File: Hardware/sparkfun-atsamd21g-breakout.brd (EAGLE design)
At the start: 17.8 x 33 mm, 41 parts, among them Q1 2N7002PW, Q3 2.5A/30V, U1 ATSAMD21G-A, U2 MIC5219 3.3V, U4 74AHC1G125

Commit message: Minor, pre-checklist modifications.
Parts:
- C5, C6: value 22pF -> 15pF; device SparkFun-Capacitors:0402-CAP -> samd21-temp:0402-CAP
- D1: value Yellow -> GREEN
- D4: value GREEN -> Yellow
- Y1: value (none) -> 32.768kHz
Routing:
- net SDA: track 9.45 -> 8.50 mm
- net D5: track 15.0 -> 14.3 mm
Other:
- board text added: "This is a 4-layer board!"

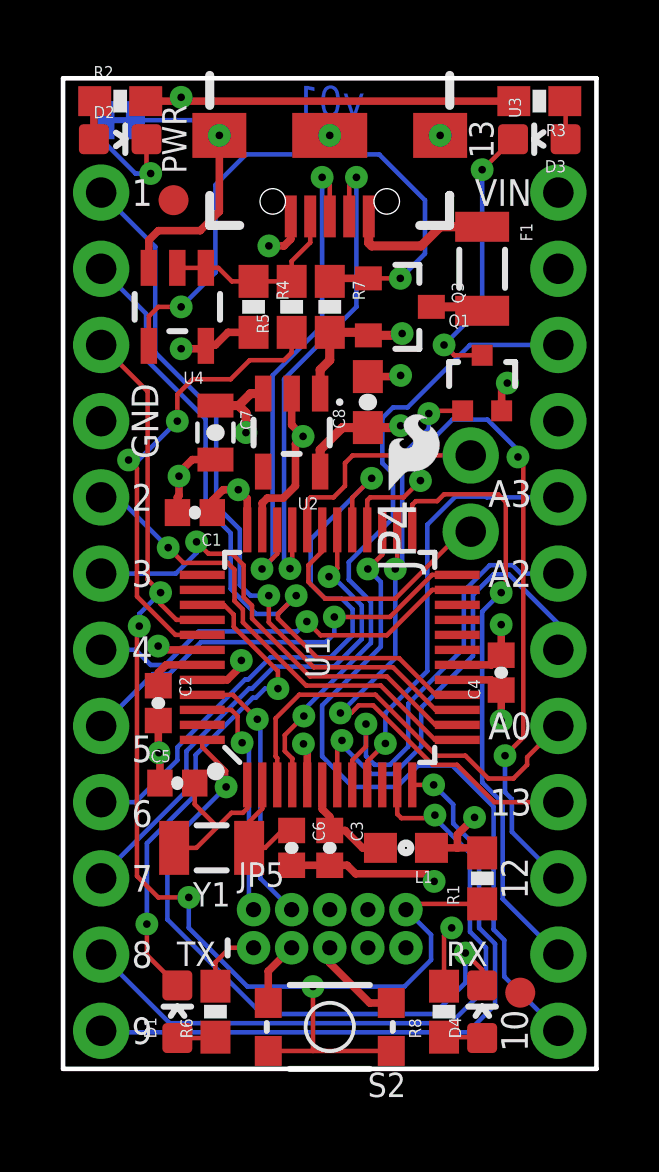
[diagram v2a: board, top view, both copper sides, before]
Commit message: Renaming U4 to U3, adding tSilk to pin 11, dimension to .008in.
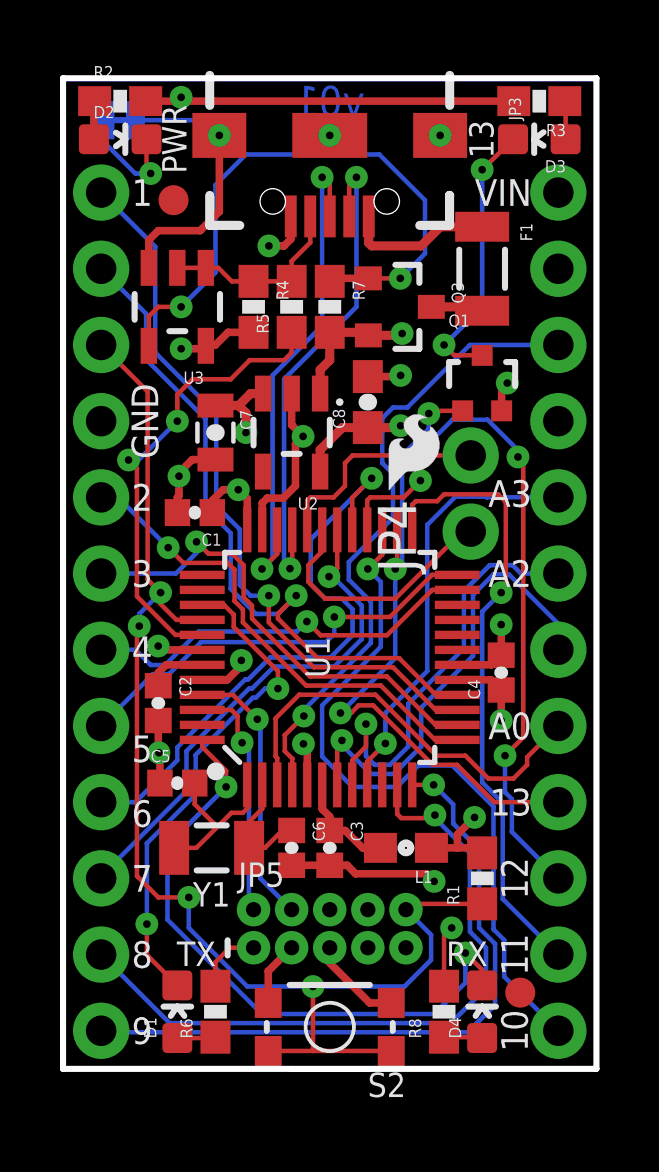
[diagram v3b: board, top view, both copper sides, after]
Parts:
- removed U4: 74AHC1G125, SparkFun-DigitalIC:SOT23-5
- added JP3: (no value), SparkFun-Connectors:USB-AB-MICRO-SMD_V03
- U3: value (none) -> 74AHC1G125; device SparkFun-Connectors:USB-AB-MICRO-SMD_V03 -> SparkFun-DigitalIC:SOT23-5
- moved U3 7.65 mm to (3.81, 25.4), turned to 180 degrees
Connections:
- net 3.3V: now also U3.5; no longer U4.5
- net GND: now also JP3.GND1, JP3.SHIELD1, JP3.SHIELD2, JP3.SHIELD3, U3.3; no longer U3.GND1, U3.SHIELD1, U3.SHIELD2, U3.SHIELD3, U4.3
- net N$1: now also JP3.VBUS1; no longer U3.VBUS1
- net N$8: now also JP3.ID1, U3.1, U3.2; no longer U3.ID1, U4.1, U4.2
- net N$9: now also U3.4; no longer U4.4
- net USB_D+: now also JP3.D+1; no longer U3.D+1
- net USB_D-: now also JP3.D-1; no longer U3.D-1
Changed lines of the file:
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@@
 <setting verticaltext="up"/>
 </settings>
-<grid distance="0.05" unitdist="inch" unit="inch" style="lines" multiple="1" display="yes" altdistance="0.0025" altunitdist="inch" altunit="inch"/>
+<grid distance="0.05" unitdist="inch" unit="inch" style="lines" multiple="1" display="yes" altdistance="0.005" altunitdist="inch" altunit="inch"/>
 <layers>
 <layer number="1" name="Top" color="4" fill="1" visible="yes" active="yes"/>
@@
 <layer number="47" name="Measures" color="7" fill="1" visible="no" active="yes"/>
 <layer number="48" name="Document" color="7" fill="1" visible="no" active="yes"/>
-<layer number="49" name="Reference" color="7" fill="1" visible="yes" active="yes"/>
+<layer number="49" name="Reference" color="7" fill="1" visible="no" active="yes"/>
 <layer number="50" name="dxf" color="7" fill="1" visible="no" active="no"/>
 <layer number="51" name="tDocu" color="6" fill="1" visible="yes" active="yes"/>
@@
 <board>
 <plain>
-<wire x1="0" y1="0" x2="0" y2="33.02" width="0.1524" layer="20"/>
-<wire x1="0" y1="33.02" x2="17.78" y2="33.02" width="0.1524" layer="20"/>
-<wire x1="17.78" y1="33.02" x2="17.78" y2="0" width="0.1524" layer="20"/>
-<wire x1="17.78" y1="0" x2="0" y2="0" width="0.1524" layer="20"/>
+<wire x1="0" y1="0" x2="0" y2="33.02" width="0.2032" layer="20"/>
+<wire x1="0" y1="33.02" x2="17.78" y2="33.02" width="0.2032" layer="20"/>
+<wire x1="17.78" y1="33.02" x2="17.78" y2="0" width="0.2032" layer="20"/>
+<wire x1="17.78" y1="0" x2="0" y2="0" width="0.2032" layer="20"/>
 <text x="2.286" y="29.21" size="0.889" layer="21" font="vector" ratio="15" align="center-left">1</text>
 <text x="2.286" y="21.59" size="0.889" layer="21" font="vector" ratio="15" rot="R270" align="bottom-center">GND</text>
@@
 <text x="8.89" y="32.766" size="1.016" layer="16" font="vector" ratio="15" rot="MR0" align="top-center">v01</text>
 <text x="8.89" y="35.56" size="0.889" layer="51" font="vector" ratio="15" align="bottom-center">This is a 4-layer board!</text>
+<text x="15.494" y="3.81" size="0.889" layer="21" font="vector" ratio="15" rot="R90" align="bottom-center">11</text>
 </plain>
 <attributes>
@@
 <attribute name="PROD_ID" value="RES-11150" x="13.97" y="26.67" size="0.889" layer="27" font="vector" ratio="15" rot="R270" display="off"/>
 </element>
-<element name="U3" library="SparkFun-Connectors" package="USB-AB-MICRO-SMD_V03" value="" x="8.89" y="31.115" rot="R270">
+<element name="JP3" library="SparkFun-Connectors" package="USB-AB-MICRO-SMD_V03" value="" x="8.89" y="31.115" rot="R270">
 <attribute name="PROD_ID" value="CONN-11794" x="8.89" y="31.115" size="0.889" layer="27" font="vector" ratio="15" rot="R270" display="off"/>
 </element>
-<element name="U4" library="SparkFun-DigitalIC" package="SOT23-5" value="74AHC1G125" x="3.81" y="25.4" rot="R180">
+<element name="U3" library="SparkFun-DigitalIC" package="SOT23-5" value="74AHC1G125" x="3.81" y="25.4" rot="R180">
 <attribute name="PROD_ID" value="IC-11920" x="3.81" y="25.4" size="0.889" layer="27" font="vector" ratio="15" rot="R180" display="off"/>
 </element>
@@
 <contactref element="JP5" pad="5"/>
 <contactref element="JP5" pad="3"/>
-<contactref element="U3" pad="GND1"/>
-<contactref element="U3" pad="SHIELD1"/>
-<contactref element="U3" pad="SHIELD2"/>
-<contactref element="U3" pad="SHIELD3"/>
-<contactref element="U4" pad="3"/>
+<contactref element="JP3" pad="GND1"/>
+<contactref element="JP3" pad="SHIELD1"/>
+<contactref element="JP3" pad="SHIELD2"/>
+<contactref element="JP3" pad="SHIELD3"/>
+<contactref element="U3" pad="3"/>
 <via x="8.001" y="21.082" extent="1-16" drill="0.254"/>
 <via x="11.2522" y="23.114" extent="1-16" drill="0.254"/>
@@
 <contactref element="JP5" pad="1"/>
 <contactref element="R4" pad="2"/>
-<contactref element="U4" pad="5"/>
+<contactref element="U3" pad="5"/>
 <via x="11.2522" y="21.4376" extent="1-16" drill="0.254"/>
 <wire x1="6.14" y1="17.966" x2="6.14" y2="19.006" width="0.254" layer="1"/>
@@
 <signal name="USB_D+">
 <contactref element="U1" pad="34"/>
-<contactref element="U3" pad="D+1"/>
+<contactref element="JP3" pad="D+1"/>
 <wire x1="8.89" y1="28.415" x2="8.89" y2="29.464" width="0.1524" layer="1"/>
 <via x="8.636" y="29.718" extent="1-16" drill="0.254"/>
@@
 <signal name="USB_D-">
 <contactref element="U1" pad="33"/>
-<contactref element="U3" pad="D-1"/>
+<contactref element="JP3" pad="D-1"/>
 <wire x1="9.54" y1="28.415" x2="9.54" y2="29.479" width="0.1524" layer="1"/>
 <wire x1="9.54" y1="29.479" x2="9.779" y2="29.718" width="0.1524" layer="1"/>
@@
 <signal name="N$1">
 <contactref element="F1" pad="1"/>
-<contactref element="U3" pad="VBUS1"/>
+<contactref element="JP3" pad="VBUS1"/>
 <wire x1="10.19" y1="28.415" x2="10.19" y2="27.529" width="0.3048" layer="1"/>
 <wire x1="10.19" y1="27.529" x2="10.287" y2="27.432" width="0.3048" layer="1"/>
@@
 </signal>
 <signal name="N$8">
-<contactref element="U4" pad="1"/>
-<contactref element="U4" pad="2"/>
+<contactref element="U3" pad="1"/>
+<contactref element="U3" pad="2"/>
 <contactref element="R4" pad="1"/>
 <contactref element="R5" pad="2"/>
-<contactref element="U3" pad="ID1"/>
+<contactref element="JP3" pad="ID1"/>
 <wire x1="8.24" y1="28.415" x2="8.24" y2="27.544" width="0.1524" layer="1"/>
 <wire x1="8.24" y1="27.544" x2="7.62" y2="26.924" width="0.1524" layer="1"/>
@@
 </signal>
 <signal name="N$9">
-<contactref element="U4" pad="4"/>
+<contactref element="U3" pad="4"/>
 <contactref element="Q3" pad="1"/>
 <contactref element="R7" pad="1"/>
